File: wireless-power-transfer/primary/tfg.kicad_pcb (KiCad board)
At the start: 2 copper layers, 160 x 100 mm, 56 parts, among them J1 CONN_01X06, J2 Screw_Terminal_1x02, J3 BARREL_JACK, Q1 IRLB8721PBF, Q2 IRLB8721PBF, Q3 IRLB8721PBF, Q4 IRLB8721PBF, U1 PIC18F45K20-I/PT, U2 IR2110, U3 IR2110, U4 R-78E15, U5 R-78E3.3, U6 XBEE_Wi-Fi

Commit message: Second version of primary PCB.
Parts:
- moved C2 6.71 mm to (202.6, 110.8), turned to 90 degrees
- moved C1 6.34 mm to (206.6, 110.8), turned to 90 degrees
- moved SW_POW1 1.35 mm to (202.2, 46.0)
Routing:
- net Net-(J1-Pad5): track 22.4 -> 41.0 mm
- net /+3.3V: track 258.8 -> 266.7 mm
- net Net-(C1-Pad2): track 586.7 -> 582.4 mm
- net Net-(J1-Pad1): track 30.7 -> 27.4 mm, vias 0 -> 1
- net Net-(U1-Pad44): track 105.1 -> 103.6 mm
- net Net-(U1-Pad2): track 119.2 -> 117.7 mm
- net Net-(J3-Pad1): track 12.2 -> 10.9 mm
- net Net-(U1-Pad1): track 99.9 -> 98.6 mm
- net Net-(J1-Pad4): track 22.4 -> 23.5 mm
- net Net-(C5-Pad1): track 96.9 -> 95.8 mm

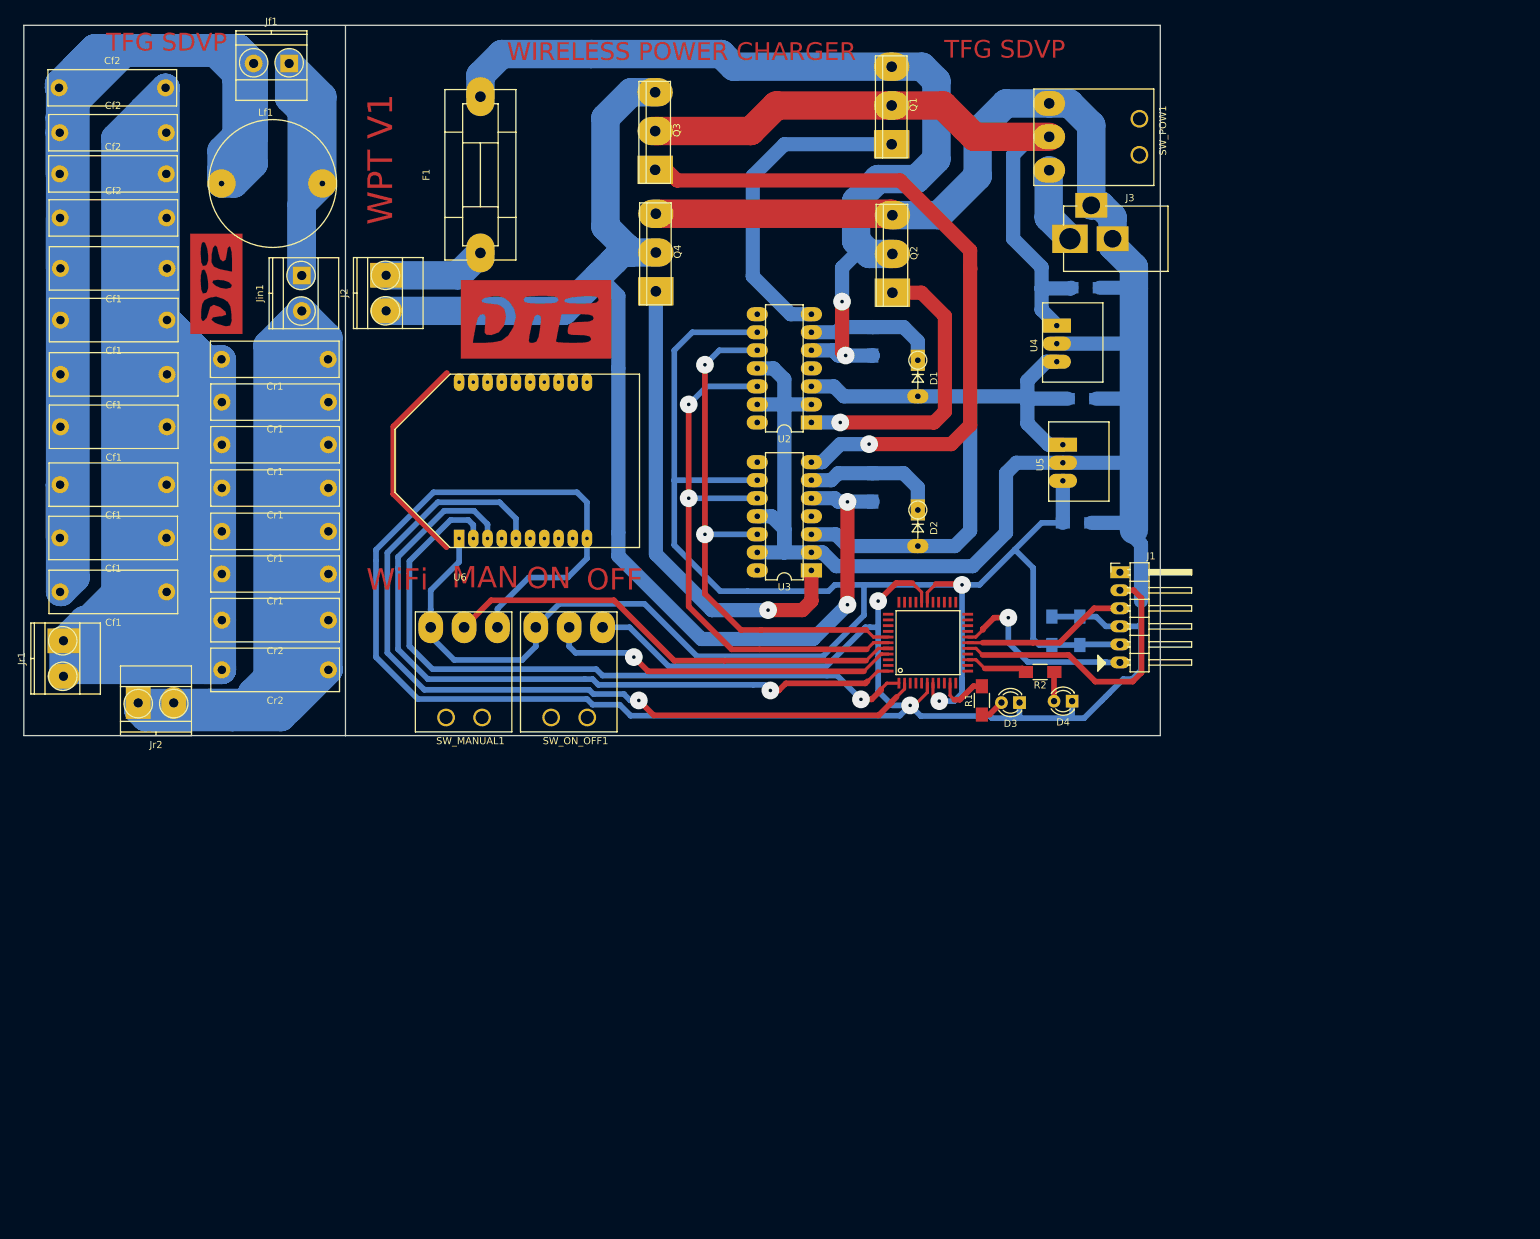
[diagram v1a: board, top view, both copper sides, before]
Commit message: Added resistor between pins 1 and 2 of the PicKit connector.
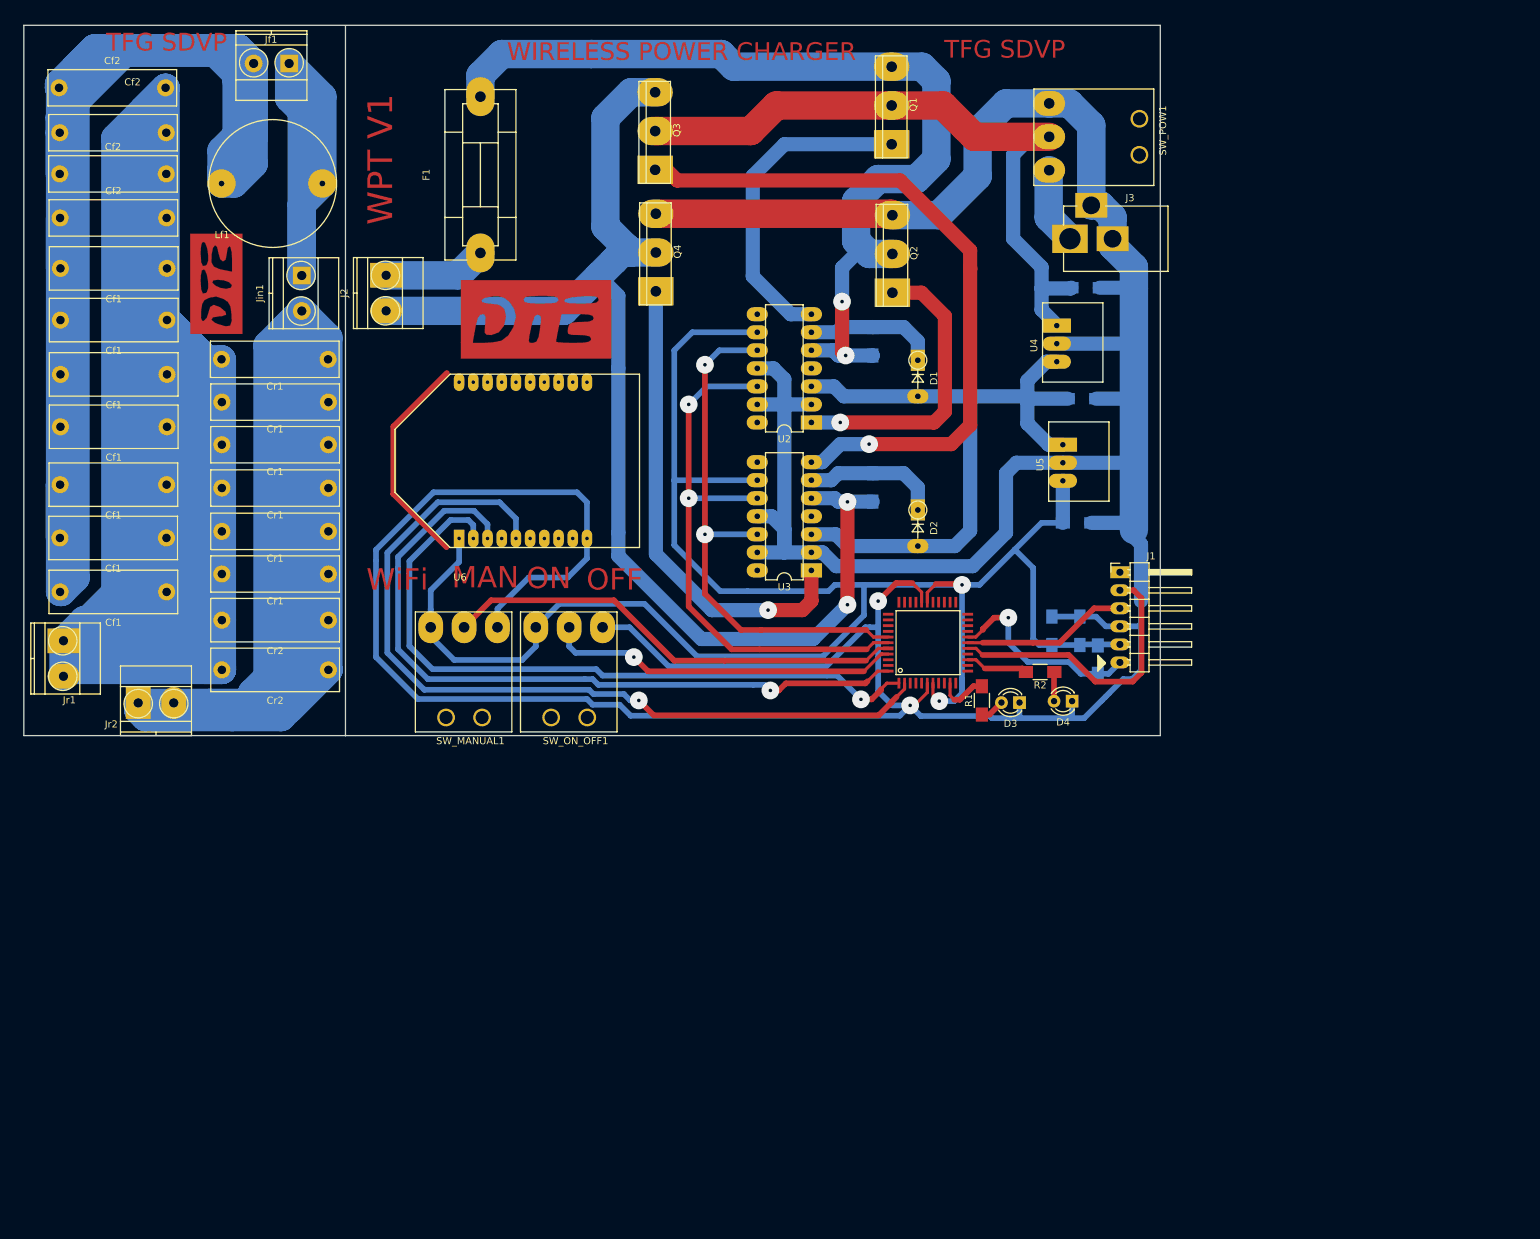
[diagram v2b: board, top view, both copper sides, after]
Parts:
- added Rpu1: 10k, Resistors_SMD:R_1206_HandSoldering, B.Cu at (209.1, 114.9)
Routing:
- net Net-(J1-Pad1): track 27.4 -> 28.6 mm

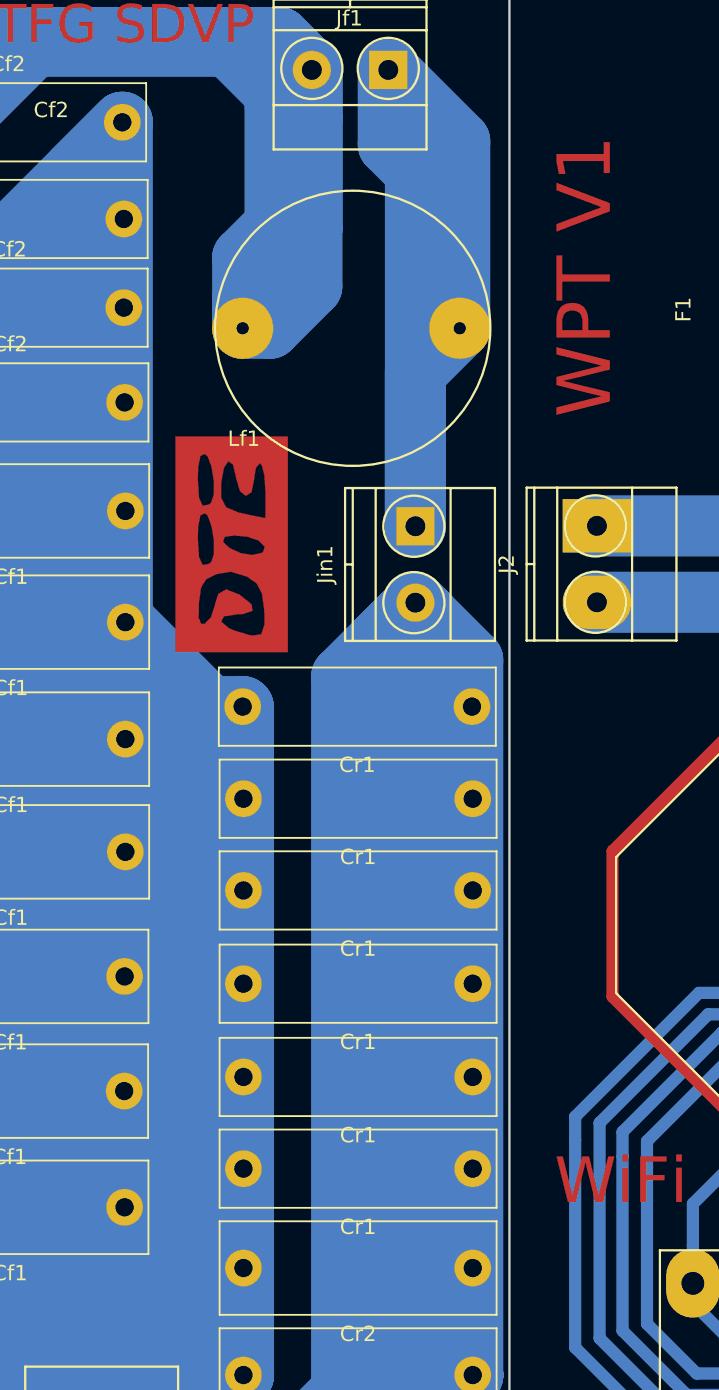
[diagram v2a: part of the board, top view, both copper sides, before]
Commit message: The two PCBs of the primary circuit have been connected.
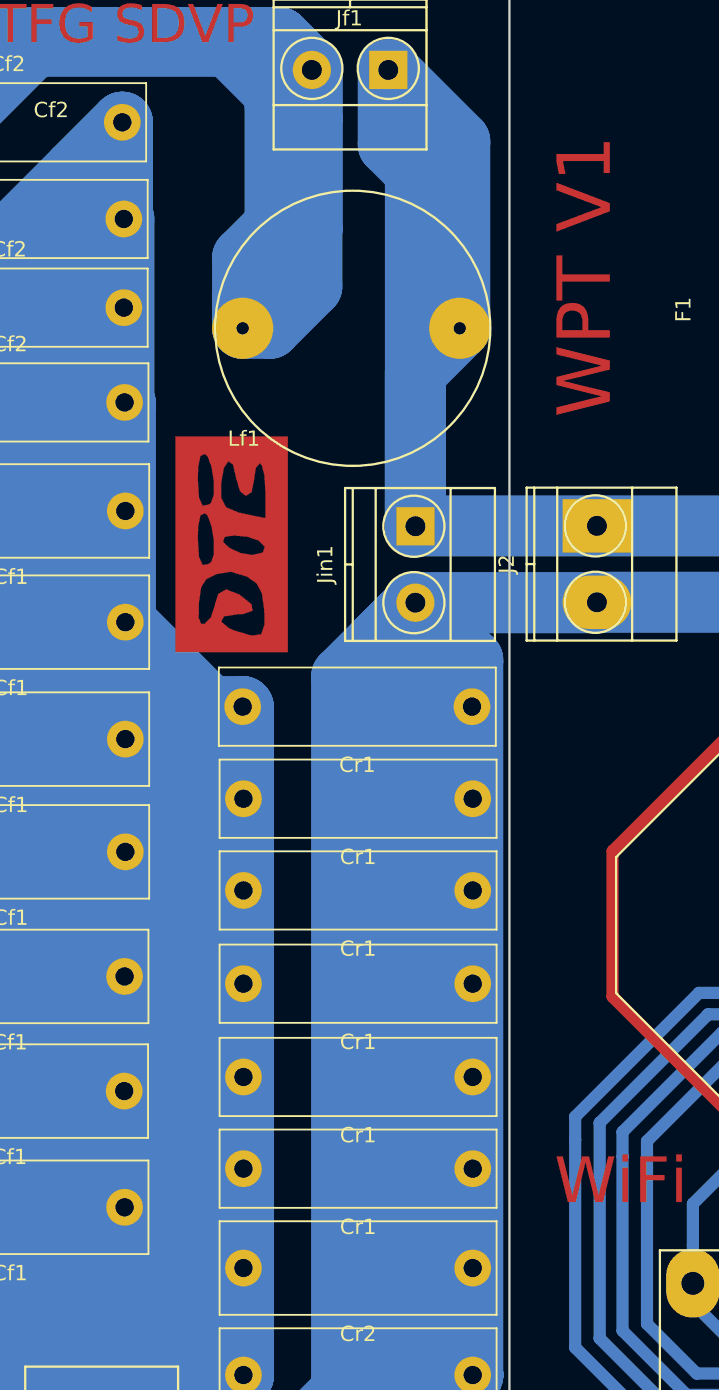
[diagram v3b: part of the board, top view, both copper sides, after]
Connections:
- Cboot2 pad 2: Net-(Cboot2-Pad2) -> Carga0
- Cr1 pad 1: Net-(Cr1-Pad1) -> Carga0
- Cr2 pad 1: Net-(Cr1-Pad1) -> Carga0
- F1 pad 1: Net-(F1-Pad1) -> Carga1
- J2 pad 1: Net-(F1-Pad1) -> Carga1
- J2 pad 2: Net-(Cboot2-Pad2) -> Carga0
- Jf1 pad 1: Net-(Jf1-Pad1) -> Carga1
- Jin1 pad 1: Net-(Jf1-Pad1) -> Carga1
- Jin1 pad 2: Net-(Cr1-Pad1) -> Carga0
- Jr2 pad 1: Net-(Cr1-Pad1) -> Carga0
- Jr2 pad 2: Net-(Cr1-Pad1) -> Carga0
- Lf1 pad 1: Net-(Jf1-Pad1) -> Carga1
- Q3 pad 3: Net-(Cboot2-Pad2) -> Carga0
- Q4 pad 2: Net-(Cboot2-Pad2) -> Carga0
- U3 pad 5: Net-(Cboot2-Pad2) -> Carga0
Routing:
- net Carga0: track 0.00 -> 505.7 mm, vias 0 -> 2
- net Net-(Cr1-Pad1): track 312.5 -> 0.00 mm
- net Net-(Cboot2-Pad2): track 173.1 -> 0.00 mm, vias 2 -> 0
- net Net-(Cf1-Pad1): track 531.4 -> 666.9 mm
- net Carga1: track 0.00 -> 90.0 mm
- net Net-(Jf1-Pad1): track 63.6 -> 0.00 mm
- net Net-(F1-Pad1): track 14.6 -> 0.00 mm

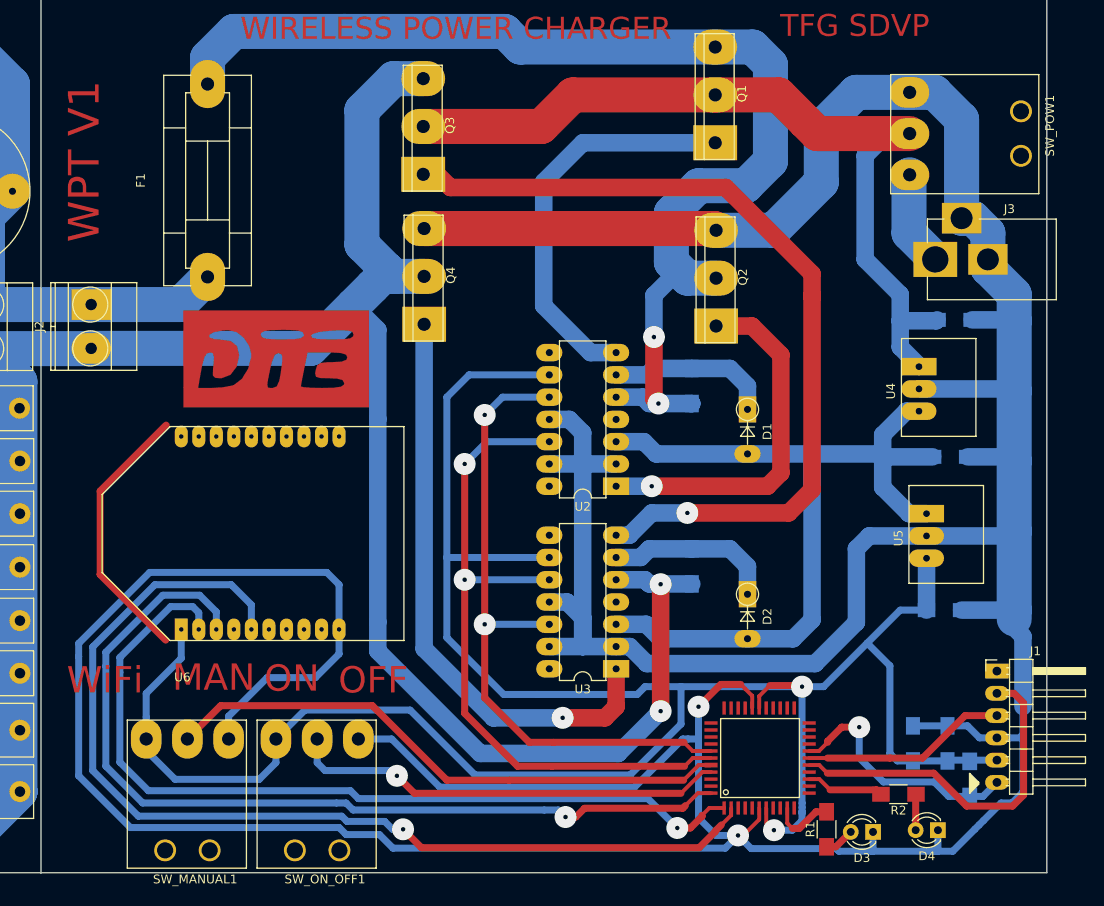
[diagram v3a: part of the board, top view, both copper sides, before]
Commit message: Minor changes on Silk layer.
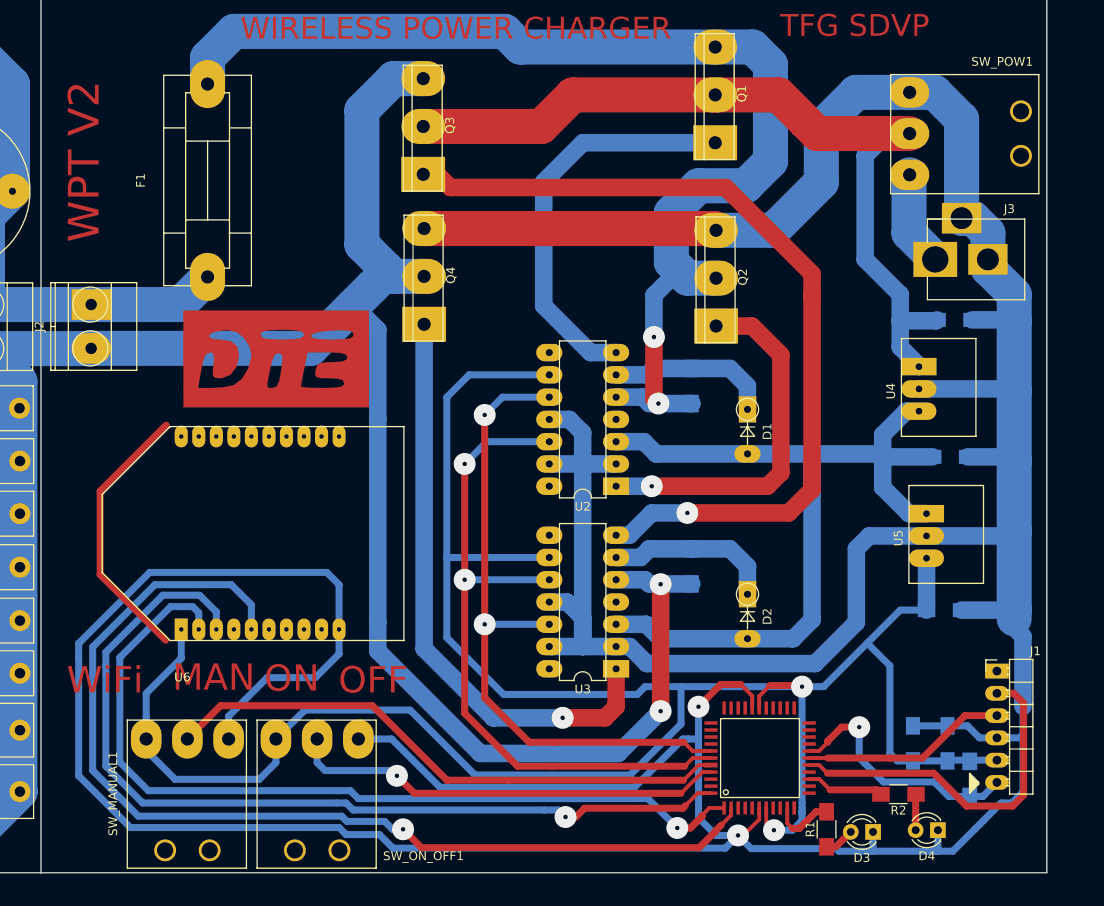
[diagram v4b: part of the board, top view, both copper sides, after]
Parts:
- J1: footprint Pin_Headers:Pin_Header_Angled_1x06_Pitch2.54mm -> Pin_Header_Angled_1x06_Pitch2.54mm
- J3: footprint Connectors:BARREL_JACK -> BARREL_JACK
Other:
- board text added: "WPT V2"
- board text removed: "WPT V1"
